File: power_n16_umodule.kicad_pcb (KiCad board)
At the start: 4 copper layers, 44.8 x 41.5 mm, 25 parts, among them J1 LSHM-140-04.0-L-DV-A-N-K-TR, U1 LTM4651

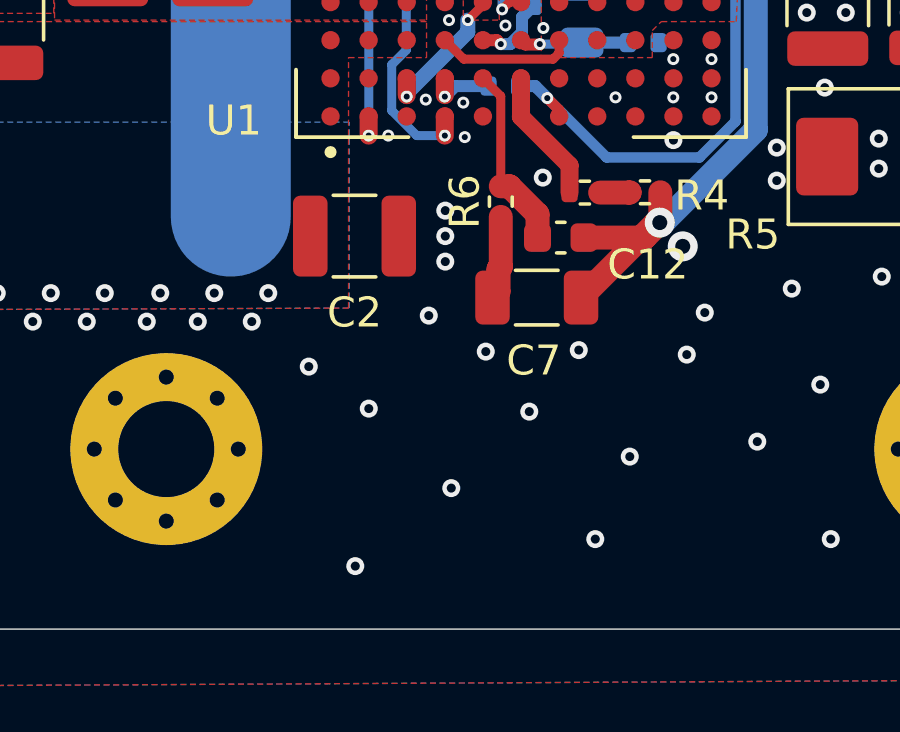
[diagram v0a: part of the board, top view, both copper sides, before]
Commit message: Add Ferrite Beads
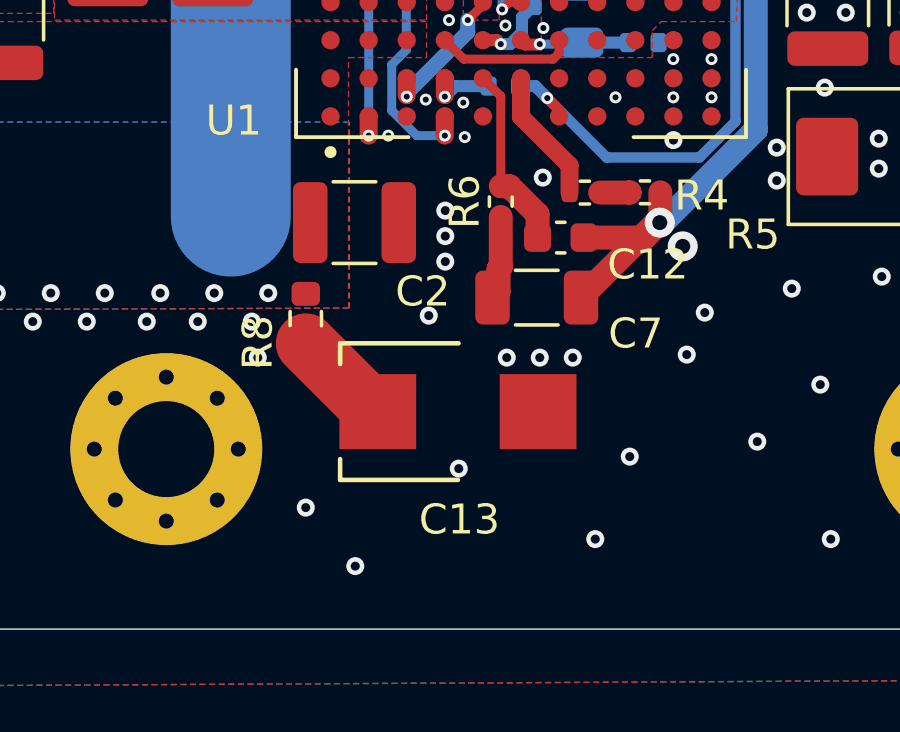
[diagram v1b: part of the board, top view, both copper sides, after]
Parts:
- added C13: 100u, lib:T521X, F.Cu at (140.7, 75.8)
- added R8: 0.5, Resistor_SMD:R_0603_1608Metric, F.Cu at (135.6, 72.7)
- moved C2 0.45 mm to (137.2, 69.5)
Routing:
- net /cf1: track 0.00 -> 3.34 mm

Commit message: Update
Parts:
- U1: value LTM4651 -> BGA77C127P7X11_900X1500X521N
